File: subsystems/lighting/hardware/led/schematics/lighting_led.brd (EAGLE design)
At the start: 44.5 x 63.5 mm, 17 parts, among them J1 MOLEX-MICROLOCK-6PIN, J2 MOLEX-MICROLOCK-6PIN

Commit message: Lighting V0.3
Fixed daisy-chaining "mirroring" problem
Made DC jack footprint holes smaller (3.3mm->3.1mm dia.)
Made Molex support pads NC
Minor routing updates
Updated silkscreen text
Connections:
- removed net N$17: J1.7, J1.8, J2.7, J2.8
- net N$16: now also J2.1; no longer J2.6
- net N$18: now also J2.2; no longer J2.5
- net N$19: now also J2.3; no longer J2.4
- net N$20: now also J2.4; no longer J2.3
- net N$21: now also J2.5; no longer J2.2
- net N$22: now also J2.6; no longer J2.1
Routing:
- net N$17: track 92.6 -> 0.00 mm, vias 2 -> 0
- net N$22: track 32.1 -> 22.1 mm, vias 2 -> 0
- net N$18: track 33.0 -> 23.4 mm, vias 2 -> 0
- net N$16: track 75.8 -> 66.5 mm
- net N$19: track 23.5 -> 15.4 mm, vias 2 -> 0
- net N$21: track 21.4 -> 14.9 mm, vias 2 -> 0
- net N$14: track 17.3 -> 15.4 mm
- net N$15: track 24.4 -> 23.4 mm
- net N$12: track 15.4 -> 14.8 mm
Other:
- board text added: "PeaPod Lighting LED Board V0.3"
- board text removed: "PeaPod Lighting LED Board V0.2"

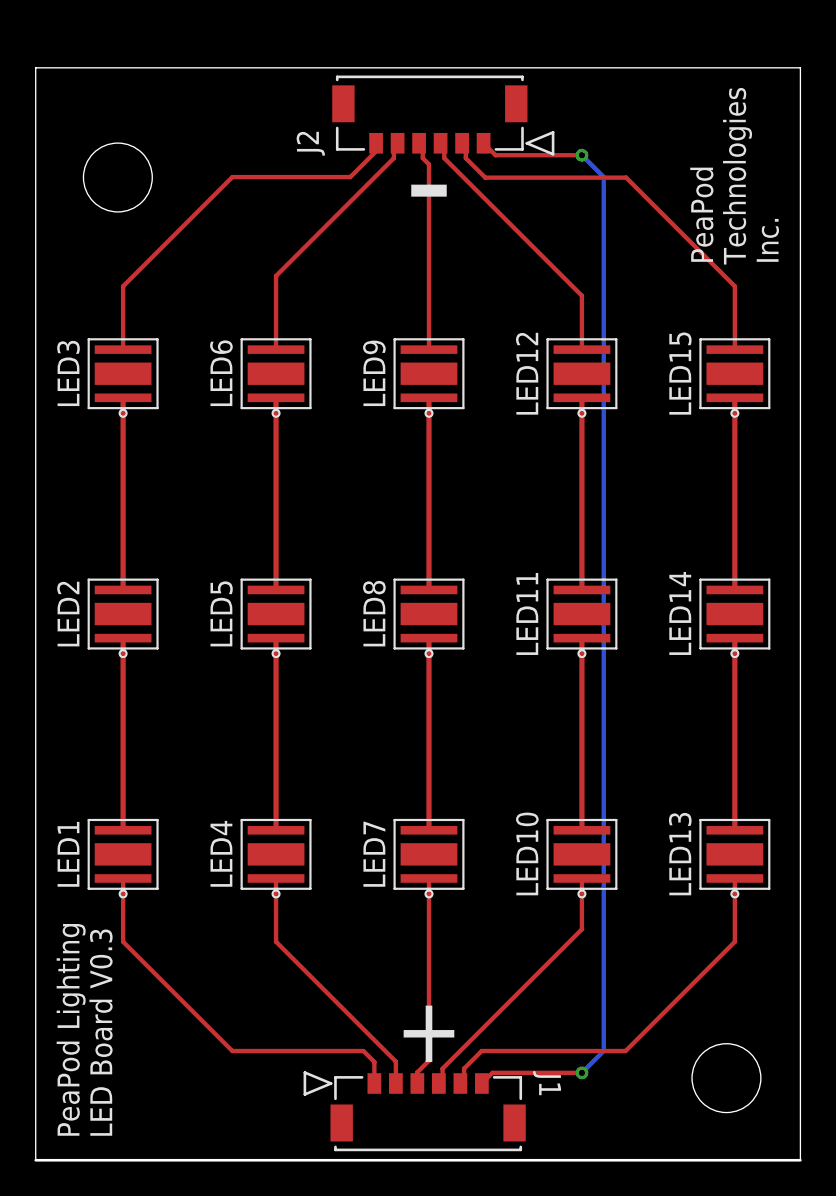
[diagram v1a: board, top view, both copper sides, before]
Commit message: Lighting V0.4
FINALLY fixed the connector flipping error (hint: pin 1 goes to pin 6 EVERY TIME)
Flipped LED series order (blue on bottom)
More "bus"-like routing on power PCB
Updated version number text on PCBs
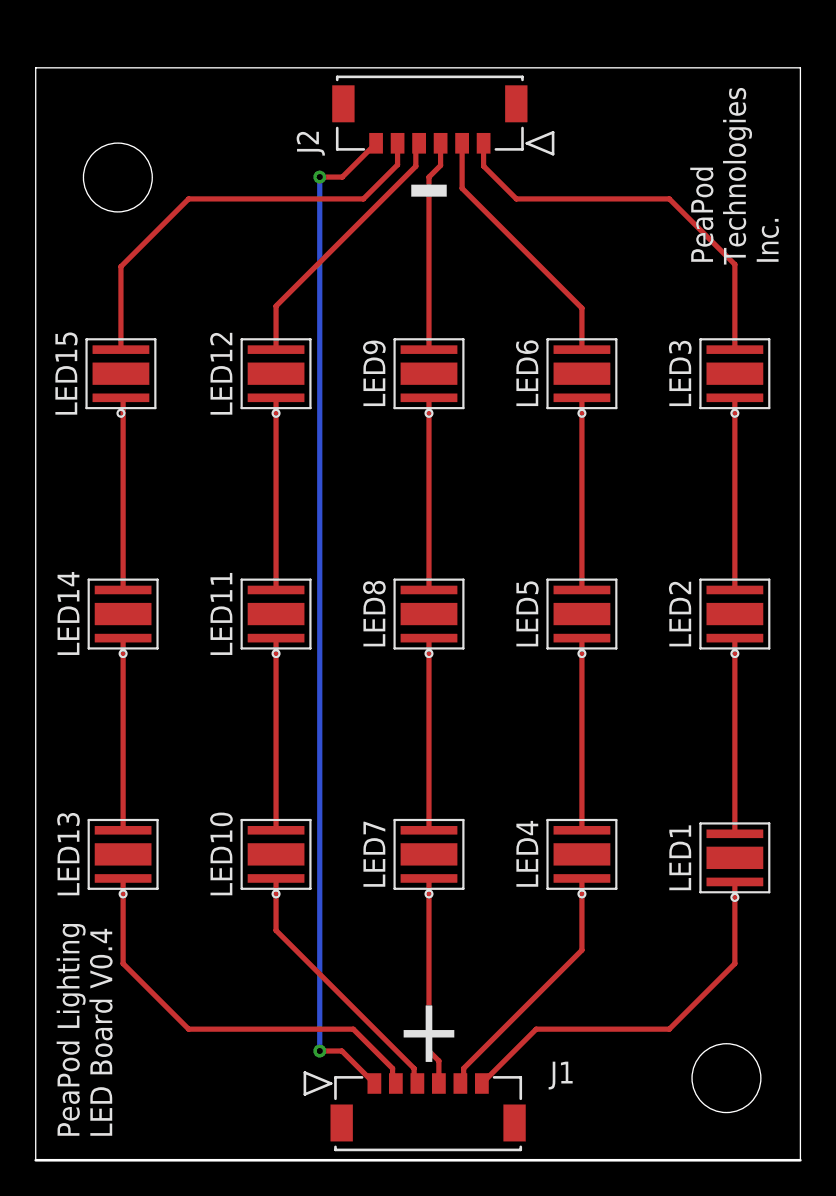
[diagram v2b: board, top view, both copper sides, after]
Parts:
- moved LED15 35.7 mm to (3.68, 48.3)
- moved LED1 35.6 mm to (39.4, 20.1)
- moved LED13 35.6 mm to (3.81, 20.3)
- moved LED14 35.6 mm to (3.81, 34.3)
- moved LED2 35.6 mm to (39.4, 34.3)
- moved LED3 35.6 mm to (39.4, 48.3)
- moved LED10 17.8 mm to (12.7, 20.3)
- moved LED11 17.8 mm to (12.7, 34.3)
- moved LED12 17.8 mm to (12.7, 48.3)
- moved LED4 17.8 mm to (30.5, 20.3)
- moved LED5 17.8 mm to (30.5, 34.3)
- moved LED6 17.8 mm to (30.5, 48.3)
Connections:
- net N$11: now also J1.6; no longer J1.1
- net N$12: now also J1.5; no longer J1.2
- net N$13: now also J1.4; no longer J1.3
- net N$14: now also J1.3; no longer J1.4
- net N$15: now also J1.2; no longer J1.5
- net N$16: now also J1.1, J2.6; no longer J1.6, J2.1
- net N$18: now also J2.5; no longer J2.2
- net N$19: now also J2.4; no longer J2.3
- net N$20: now also J2.3; no longer J2.4
- net N$21: now also J2.2; no longer J2.5
- net N$22: now also J2.1; no longer J2.6
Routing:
- net N$16: track 66.5 -> 58.8 mm
- net N$18: track 23.4 -> 24.6 mm
- net N$22: track 22.1 -> 23.3 mm
- net N$15: track 23.4 -> 24.1 mm
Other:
- board text added: "PeaPod Lighting LED Board V0.4"
- board text removed: "PeaPod Lighting LED Board V0.3"
